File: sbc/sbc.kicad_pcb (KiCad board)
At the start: 4 copper layers, 111.8 x 76.2 mm, 38 parts, among them J1 USB_B_Micro, J2 EXP_1A, J3 EXP_1B, J4 EXP_2A, J5 EXP_2B, M1 M2, M2 M2, M3 M2, M4 M2, SW1 RESET, SW2 NMI, U1 DS1813, U2 WD65C02, U3 28C256, U4 62256, U5 7400, U6 WD65C22, U7 WD65C22, U8 74AHC1G08, U9 MAX6816, X1 2Mhz

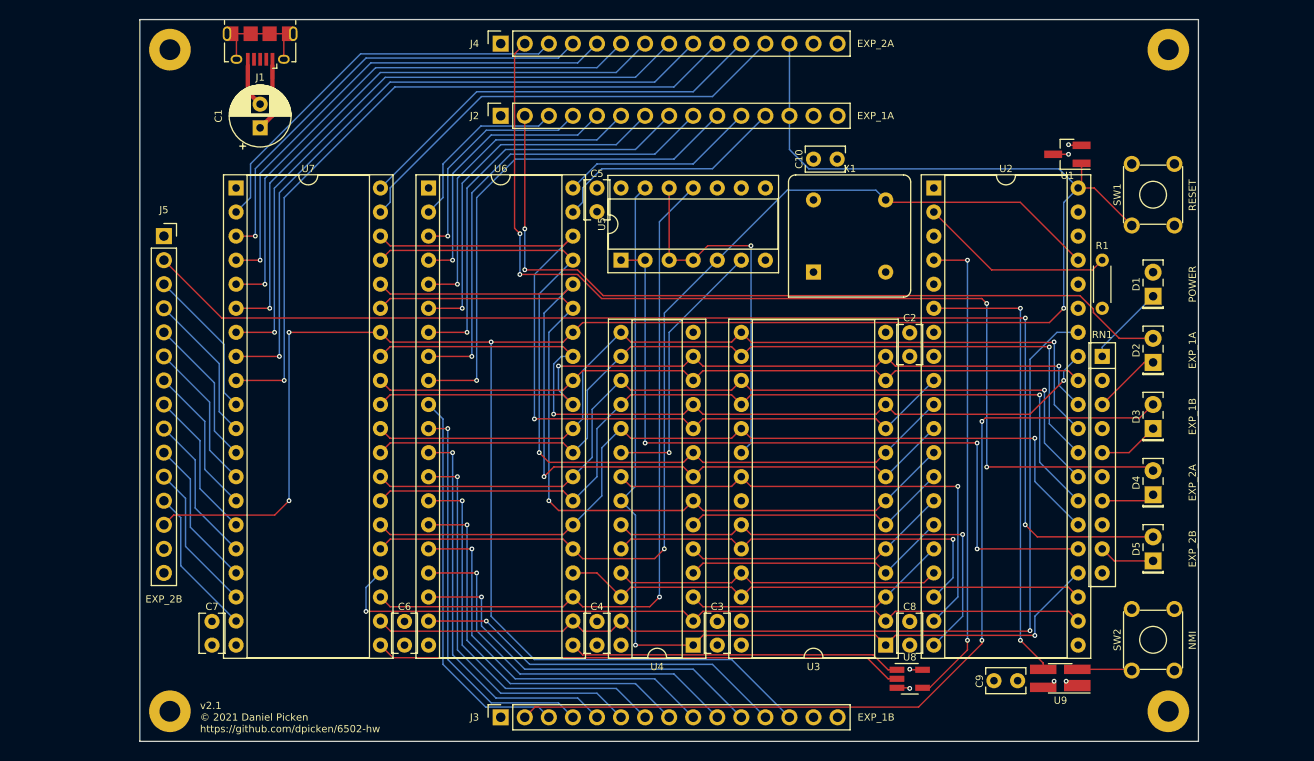
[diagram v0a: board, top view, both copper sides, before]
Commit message: SBC v2.2
Changes over v2:

  - Address space decode and IRQ glue logic moved into a PLD
  - Adds serial port and power via USB-C connector
  - Adds onboard microSD mass storage
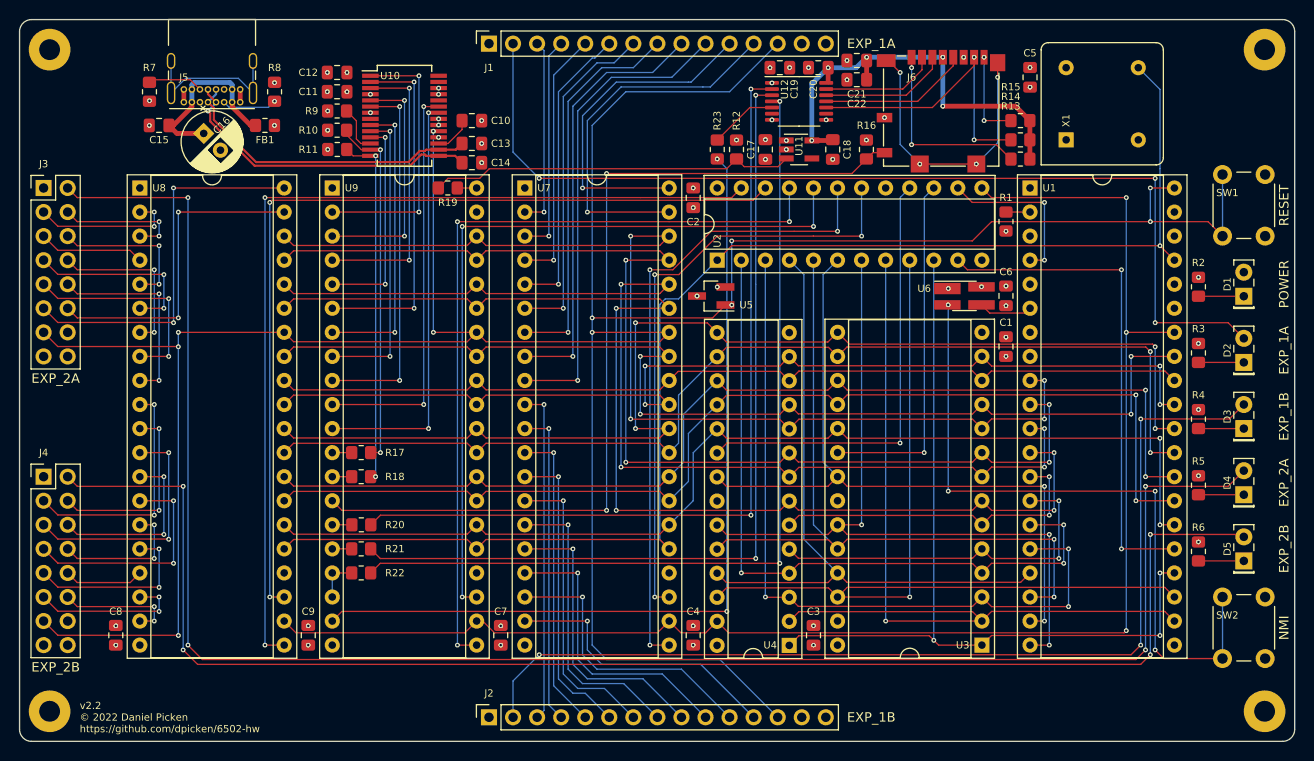
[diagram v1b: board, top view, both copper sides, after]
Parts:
- removed M1, M2, M3, M4: M2, mounting_hole:MountingHole_2.2mm_M2_Pad
- removed RN1: 100, resistor:R_Array_SIP10
- added C11: 0.1uF, Capacitor_SMD:C_0805_2012Metric_Pad1.18x1.45mm_HandSolder, F.Cu at (117.3, 58.4)
- added C12: 4.7uF, Capacitor_SMD:C_0805_2012Metric_Pad1.18x1.45mm_HandSolder, F.Cu at (117.3, 56.4)
- added C13: 47pF, Capacitor_SMD:C_0805_2012Metric_Pad1.18x1.45mm_HandSolder, F.Cu at (131.6, 63.9)
- added C14: 47pF, Capacitor_SMD:C_0805_2012Metric_Pad1.18x1.45mm_HandSolder, F.Cu at (131.6, 65.9)
- added C15: 10nF, Capacitor_SMD:C_0805_2012Metric_Pad1.18x1.45mm_HandSolder, F.Cu at (98.6, 62.0)
- added C16: 220uF, Capacitor_THT:CP_Radial_D6.3mm_P2.50mm, F.Cu at (103.3, 62.8)
- added C17: 1uF, Capacitor_SMD:C_0805_2012Metric_Pad1.18x1.45mm_HandSolder, F.Cu at (162.6, 64.5)
- added C18: 1uF, Capacitor_SMD:C_0805_2012Metric_Pad1.18x1.45mm_HandSolder, F.Cu at (169.7, 64.5)
- added C19: 0.1uF, Capacitor_SMD:C_0805_2012Metric_Pad1.18x1.45mm_HandSolder, F.Cu at (164.1, 55.9)
- added C20: 0.1uF, Capacitor_SMD:C_0805_2012Metric_Pad1.18x1.45mm_HandSolder, F.Cu at (168.1, 55.9)
- added C21: 0.1uF, Capacitor_SMD:C_0805_2012Metric_Pad1.18x1.45mm_HandSolder, F.Cu at (172.2, 55.1)
- added C22: 4.7uF, Capacitor_SMD:C_0805_2012Metric_Pad1.18x1.45mm_HandSolder, F.Cu at (172.2, 57.1)
- added FB1: FerriteBead, Resistor_SMD:R_0805_2012Metric_Pad1.20x1.40mm_HandSolder, F.Cu at (109.7, 62.0)
- added H1: MountingHole, MountingHole:MountingHole_2.2mm_M2_Pad, F.Cu at (87.0, 54.0)
- added H2: MountingHole, MountingHole:MountingHole_2.2mm_M2_Pad, F.Cu at (87.0, 123.8)
- added H3: MountingHole, MountingHole:MountingHole_2.2mm_M2_Pad, F.Cu at (215.3, 123.8)
- added H4: MountingHole, MountingHole:MountingHole_2.2mm_M2_Pad, F.Cu at (215.3, 54.0)
- added J6: 104031-0811, Project_Connector_Card:microSD_HC_Molex_104031-0811_HandSoler, F.Cu at (181.1, 60.5)
- added R10: 10K, Resistor_SMD:R_0805_2012Metric_Pad1.20x1.40mm_HandSolder, F.Cu at (117.3, 62.5)
- added R11: 10K, Resistor_SMD:R_0805_2012Metric_Pad1.20x1.40mm_HandSolder, F.Cu at (117.4, 64.5)
- added R12: 10K, Resistor_SMD:R_0805_2012Metric_Pad1.20x1.40mm_HandSolder, F.Cu at (159.5, 64.5)
- added R13: 10K, Resistor_SMD:R_0805_2012Metric_Pad1.20x1.40mm_HandSolder, F.Cu at (189.5, 65.5)
- added R14: 10K, Resistor_SMD:R_0805_2012Metric_Pad1.20x1.40mm_HandSolder, F.Cu at (189.5, 63.5)
- added R15: 10K, Resistor_SMD:R_0805_2012Metric_Pad1.20x1.40mm_HandSolder, F.Cu at (189.5, 61.5)
- added R16: 10K, Resistor_SMD:R_0805_2012Metric_Pad1.20x1.40mm_HandSolder, F.Cu at (173.2, 64.5)
- added R17: 30R, Resistor_SMD:R_0805_2012Metric_Pad1.20x1.40mm_HandSolder, F.Cu at (119.9, 96.5)
- added R18: 30R, Resistor_SMD:R_0805_2012Metric_Pad1.20x1.40mm_HandSolder, F.Cu at (119.9, 99.1)
- added R19: 30R, Resistor_SMD:R_0805_2012Metric_Pad1.20x1.40mm_HandSolder, F.Cu at (129.0, 68.6)
- added R2: 150R, Resistor_SMD:R_0805_2012Metric_Pad1.20x1.40mm_HandSolder, F.Cu at (208.3, 79.0)
- added R20: 30R, Resistor_SMD:R_0805_2012Metric_Pad1.20x1.40mm_HandSolder, F.Cu at (119.9, 104.1)
- added R21: 30R, Resistor_SMD:R_0805_2012Metric_Pad1.20x1.40mm_HandSolder, F.Cu at (119.9, 106.7)
- added R22: 30R, Resistor_SMD:R_0805_2012Metric_Pad1.20x1.40mm_HandSolder, F.Cu at (119.9, 109.2)
- added R23: 30R, Resistor_SMD:R_0805_2012Metric_Pad1.20x1.40mm_HandSolder, F.Cu at (157.5, 64.5)
- added R3: 150R, Resistor_SMD:R_0805_2012Metric_Pad1.20x1.40mm_HandSolder, F.Cu at (208.3, 86.0)
- added R4: 150R, Resistor_SMD:R_0805_2012Metric_Pad1.20x1.40mm_HandSolder, F.Cu at (208.3, 93.0)
- added R5: 150R, Resistor_SMD:R_0805_2012Metric_Pad1.20x1.40mm_HandSolder, F.Cu at (208.3, 100.0)
- added R6: 150R, Resistor_SMD:R_0805_2012Metric_Pad1.20x1.40mm_HandSolder, F.Cu at (208.3, 107.0)
- added R7: 5.1K, Resistor_SMD:R_0805_2012Metric_Pad1.20x1.40mm_HandSolder, F.Cu at (97.5, 58.4)
- added R8: 5.1K, Resistor_SMD:R_0805_2012Metric_Pad1.20x1.40mm_HandSolder, F.Cu at (110.7, 58.4)
- added R9: 10K, Resistor_SMD:R_0805_2012Metric_Pad1.20x1.40mm_HandSolder, F.Cu at (117.3, 60.5)
- added U10: FT245R, Package_SO:SSOP-28_5.3x10.2mm_P0.65mm, F.Cu at (124.5, 61.0)
- added U11: LD39015M33R, Package_TO_SOT_SMD:SOT-23-5_HandSoldering, F.Cu at (166.1, 64.5)
- added U12: TXU0304, Package_SO:TSSOP-14_4.4x5mm_P0.65mm, F.Cu at (166.1, 59.4)
- C1: value 220uf -> 0.1uF; footprint capacitor:CP_Radial_D6.3mm_P2.50mm -> Capacitor_SMD:C_0805_2012Metric_Pad1.18x1.45mm_HandSolder
- C10, C3, C4, C5, C6, C7, C8, C9: footprint capacitor:C_Rect_L4.0mm_W2.5mm_P2.50mm -> Capacitor_SMD:C_0805_2012Metric_Pad1.18x1.45mm_HandSolder
- C2: value 0.1uF -> 0.22uF; footprint capacitor:C_Rect_L4.0mm_W2.5mm_P2.50mm -> Capacitor_SMD:C_0805_2012Metric_Pad1.18x1.45mm_HandSolder
- D1, D2, D3, D4, D5: footprint led:LED_Rectangular_W5.0mm_H2.0mm -> LED_THT:LED_Rectangular_W5.0mm_H2.0mm
- J1: value USB_B_Micro -> EXP_1A; footprint connector_usb_handsoldering:USB_Micro-B_Amphenol_10118194_Horizontal_HandSoldering -> Connector_PinSocket_2.54mm:PinSocket_1x15_P2.54mm_Vertical
- J2: value EXP_1A -> EXP_1B; footprint connector:PinSocket_1x15_P2.54mm_Vertical -> Connector_PinSocket_2.54mm:PinSocket_1x15_P2.54mm_Vertical
- J3: value EXP_1B -> EXP_2A; footprint connector:PinSocket_1x15_P2.54mm_Vertical -> Connector_PinHeader_2.54mm:PinHeader_2x08_P2.54mm_Vertical
- J4: value EXP_2A -> EXP_2B; footprint connector:PinSocket_1x15_P2.54mm_Vertical -> Connector_PinHeader_2.54mm:PinHeader_2x08_P2.54mm_Vertical
- J5: value EXP_2B -> USB_C_USB2.0; footprint connector:PinSocket_1x15_P2.54mm_Vertical -> Connector_USB:USB_C_Receptacle_GCT_USB4085
- R1: value 1K -> 3K; footprint resistor:R_Axial_DIN0204_L3.6mm_D1.6mm_P5.08mm_Horizontal -> Resistor_SMD:R_0805_2012Metric_Pad1.20x1.40mm_HandSolder
- SW1, SW2: footprint switch:SW_TH_Tactile_Omron_B3F-10xx -> Button_Switch_THT:SW_PUSH_6mm_H4.3mm
- U1: value DS1813 -> WD65C02; footprint to_sot_smd:SOT-23_Handsoldering -> Package_DIP:DIP-40_W15.24mm_Socket
- U2: value WD65C02 -> ATF22V10C; footprint dip:DIP-40_W15.24mm_Socket -> Package_DIP:DIP-24_W7.62mm_Socket
- U3: footprint dip:DIP-28_W15.24mm_Socket -> Package_DIP:DIP-28_W15.24mm_Socket
- U4: value 62256 -> AS7C256B; footprint dip:DIP-28_W7.62mm_Socket -> Package_DIP:DIP-28_W7.62mm_Socket
- U5: value 7400 -> DS1813; footprint dip:DIP-14_W7.62mm_Socket -> Package_TO_SOT_SMD:SOT-23_Handsoldering
- U6: value WD65C22 -> MAX6816; footprint dip:DIP-40_W15.24mm_Socket -> Package_TO_SOT_SMD:SOT-143_Handsoldering
- U7: footprint dip:DIP-40_W15.24mm_Socket -> Package_DIP:DIP-40_W15.24mm_Socket
- U8: value 74AHC1G08 -> WD65C22; footprint to_sot_smd:SOT-23-5_HandSoldering -> Package_DIP:DIP-40_W15.24mm_Socket
- U9: value MAX6816 -> WD65C22; footprint to_sot_smd:SOT-143_Handsoldering -> Package_DIP:DIP-40_W15.24mm_Socket
- X1: value 2Mhz -> 8MHz; footprint oscillator:Oscillator_DIP-8 -> Oscillator:Oscillator_DIP-8
- moved U8 96.4 mm to (96.5, 68.6)
- moved U9 92.7 mm to (116.8, 68.6), turned to 0 degrees
- moved C8 83.8 mm to (94.0, 115.8)
- moved C1 82.1 mm to (188.0, 85.3)
- moved C9 75.0 mm to (114.3, 115.8), turned to 90 degrees
- moved J3 73.8 mm to (86.4, 68.6), turned to 0 degrees
- moved C6 73.4 mm to (188.0, 80.0), turned to -90 degrees
- moved J4 66.5 mm to (86.4, 99.1), turned to 0 degrees
- moved J2 63.5 mm to (133.4, 124.5)
- moved U6 57.7 mm to (183.6, 80.0)
- moved C5 47.2 mm to (190.5, 56.9)
- moved C10 36.3 mm to (131.6, 61.5)
- moved C7 30.5 mm to (134.6, 115.8)
- moved U7 30.5 mm to (137.2, 68.6)
- moved X1 30.1 mm to (194.3, 63.5)
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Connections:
- C10 pad 1: +5V -> Net-(C10-Pad1)
- J1 pad 2: Net-(J1-Pad2) -> EXP_1A_LED
- J1 pad 3: Net-(J1-Pad3) -> VIA1_PA0
- J1 pad 4: Net-(J1-Pad4) -> VIA1_PA1
- J1 pad 5: GND -> VIA1_PA2
- J1 pad 6: Net-(J1-Pad6) -> VIA1_PA3
- J2 pad 10: VIA1_PA7 -> VIA1_PB7
- J2 pad 11: VIA1_CA1 -> VIA1_CB1
- J2 pad 12: VIA1_CA2 -> VIA1_CB2
- J2 pad 13: RESET -> /RESET
- J2 pad 15: Net-(J2-Pad15) -> unconnected-(J2-Pad15)
- J2 pad 2: EXP_1A_LED -> EXP_1B_LED
- J2 pad 3: VIA1_PA0 -> VIA1_PB0
- J2 pad 4: VIA1_PA1 -> VIA1_PB1
- J2 pad 5: VIA1_PA2 -> VIA1_PB2
- J2 pad 6: VIA1_PA3 -> VIA1_PB3
- J2 pad 7: VIA1_PA4 -> VIA1_PB4
- J2 pad 8: VIA1_PA5 -> VIA1_PB5
- J2 pad 9: VIA1_PA6 -> VIA1_PB6
- J3 pad 10: VIA1_PB7 -> VIA2_PA7
- J3 pad 11: VIA1_CB1 -> VIA2_CA1
- J3 pad 12: VIA1_CB2 -> VIA2_CA2
- J3 pad 13: RESET -> /RESET
- J3 pad 15: Net-(J3-Pad15) -> unconnected-(J3-Pad15)
- J3 pad 2: EXP_1B_LED -> EXP_2A_LED
- J3 pad 3: VIA1_PB0 -> VIA2_PA0
- J3 pad 4: VIA1_PB1 -> VIA2_PA1
- J3 pad 5: VIA1_PB2 -> VIA2_PA2
- J3 pad 6: VIA1_PB3 -> VIA2_PA3
- J3 pad 7: VIA1_PB4 -> VIA2_PA4
- J3 pad 8: VIA1_PB5 -> VIA2_PA5
- J3 pad 9: VIA1_PB6 -> VIA2_PA6
- J4 pad 10: VIA2_PA7 -> VIA2_PB7
- J4 pad 11: VIA2_CA1 -> VIA2_CB1
- J4 pad 12: VIA2_CA2 -> VIA2_CB2
- J4 pad 13: RESET -> /RESET
- J4 pad 15: Net-(J4-Pad15) -> unconnected-(J4-Pad15)
- J4 pad 2: EXP_2A_LED -> EXP_2B_LED
- J4 pad 3: VIA2_PA0 -> VIA2_PB0
- J4 pad 4: VIA2_PA1 -> VIA2_PB1
- J4 pad 5: VIA2_PA2 -> VIA2_PB2
- J4 pad 6: VIA2_PA3 -> VIA2_PB3
- J4 pad 7: VIA2_PA4 -> VIA2_PB4
- J4 pad 8: VIA2_PA5 -> VIA2_PB5
- J4 pad 9: VIA2_PA6 -> VIA2_PB6
- R1 pad 1: Net-(R1-Pad1) -> +5V
- R1 pad 2: +5V -> Net-(R1-Pad2)
- SW1 pad 1: RESET -> /RESET
- SW1 pad 2: (no net) -> GND
- SW2 pad 2: (no net) -> GND
- U1 pad 1: RESET -> unconnected-(U1-Pad1)
- U1 pad 2: +5V -> Net-(R1-Pad2)
- U1 pad 3: GND -> unconnected-(U1-Pad3)
- U2 pad 1: Net-(U2-Pad1) -> PHI2
- U2 pad 10: /A1 -> A14
- U2 pad 11: /A2 -> A15
- U2 pad 12: /A3 -> GND
- U2 pad 13: /A4 -> /W
- U2 pad 14: /A5 -> /IRQ
- U2 pad 15: /A6 -> /ROM
- U2 pad 16: /A7 -> /RAM
- U2 pad 17: /A8 -> unconnected-(U2-Pad17)
- U2 pad 18: /A9 -> /VIA1
- U2 pad 19: /A10 -> /VIA1_IRQ
- U2 pad 2: Net-(R1-Pad1) -> A6
- U2 pad 20: /A11 -> /VIA3
- U2 pad 21: GND -> /VIA3_IRQ
- U2 pad 22: /A12 -> /VIA2
- U2 pad 23: /A13 -> /VIA2_IRQ
- U2 pad 24: /A14 -> +5V
- U2 pad 3: Net-(U2-Pad3) -> A7
- U2 pad 4: IRQ -> A8
- U2 pad 5: Net-(U2-Pad5) -> A9
- U2 pad 6: NMI -> A10
- U2 pad 7: Net-(U2-Pad7) -> A11
- U2 pad 8: +5V -> A12
- U2 pad 9: /A0 -> A13
- U3 pad 1: /A14 -> A14
- U3 pad 10: /A0 -> A0
- U3 pad 11: /D0 -> D0
- U3 pad 12: /D1 -> D1
- U3 pad 13: /D2 -> D2
- U3 pad 15: /D3 -> D3
- U3 pad 16: /D4 -> D4
- U3 pad 17: /D5 -> D5
- U3 pad 18: /D6 -> D6
- U3 pad 19: /D7 -> D7
- U3 pad 2: /A12 -> A12
- U3 pad 20: Net-(U3-Pad20) -> /ROM
- U3 pad 21: /A10 -> A10
- U3 pad 23: /A11 -> A11
- U3 pad 24: /A9 -> A9
- U3 pad 25: /A8 -> A8
- U3 pad 26: /A13 -> A13
- U3 pad 3: /A7 -> A7
- U3 pad 4: /A6 -> A6
- U3 pad 5: /A5 -> A5
- U3 pad 6: /A4 -> A4
- U3 pad 7: /A3 -> A3
- U3 pad 8: /A2 -> A2
- U3 pad 9: /A1 -> A1
- U4 pad 1: /A14 -> A14
- U4 pad 10: /A0 -> A0
- U4 pad 11: /D0 -> D0
- U4 pad 12: /D1 -> D1
- U4 pad 13: /D2 -> D2
- U4 pad 15: /D3 -> D3
- U4 pad 16: /D4 -> D4
- U4 pad 17: /D5 -> D5
- U4 pad 18: /D6 -> D6
- U4 pad 19: /D7 -> D7
- U4 pad 2: /A12 -> A12
- U4 pad 20: Net-(U4-Pad20) -> /RAM
- U4 pad 21: /A10 -> A10
- U4 pad 22: /A14 -> GND
- U4 pad 23: /A11 -> A11
- U4 pad 24: /A9 -> A9
- U4 pad 25: /A8 -> A8
- U4 pad 26: /A13 -> A13
- U4 pad 27: Net-(U2-Pad34) -> /W
- U4 pad 3: /A7 -> A7
- U4 pad 4: /A6 -> A6
- U4 pad 5: /A5 -> A5
- U4 pad 6: /A4 -> A4
- U4 pad 7: /A3 -> A3
- U4 pad 8: /A2 -> A2
- U4 pad 9: /A1 -> A1
- U5 pad 1: /A15 -> /RESET
- U5 pad 2: /A15 -> +5V
- U5 pad 3: Net-(U3-Pad20) -> GND
- U6 pad 2: VIA1_PA0 -> Net-(SW2-Pad1)
- U6 pad 3: VIA1_PA1 -> /NMI
- U6 pad 4: VIA1_PA2 -> +5V
- U7 pad 10: VIA2_PB0 -> VIA1_PB0
- U7 pad 11: VIA2_PB1 -> VIA1_PB1
- U7 pad 12: VIA2_PB2 -> VIA1_PB2
- U7 pad 13: VIA2_PB3 -> VIA1_PB3
- U7 pad 14: VIA2_PB4 -> VIA1_PB4
- U7 pad 15: VIA2_PB5 -> VIA1_PB5
- U7 pad 16: VIA2_PB6 -> VIA1_PB6
- U7 pad 17: VIA2_PB7 -> VIA1_PB7
- U7 pad 18: VIA2_CB1 -> VIA1_CB1
- U7 pad 19: VIA2_CB2 -> VIA1_CB2
- U7 pad 2: VIA2_PA0 -> VIA1_PA0
- U7 pad 21: VIA2_IRQ -> /VIA1_IRQ
- U7 pad 22: Net-(U2-Pad34) -> /W
- U7 pad 23: Net-(U5-Pad11) -> /VIA1
- U7 pad 24: /A12 -> +5V
- U7 pad 25: Net-(U2-Pad37) -> PHI2
- U7 pad 26: /D7 -> D7
- U7 pad 27: /D6 -> D6
- U7 pad 28: /D5 -> D5
- U7 pad 29: /D4 -> D4
- U7 pad 3: VIA2_PA1 -> VIA1_PA1
- U7 pad 30: /D3 -> D3
- U7 pad 31: /D2 -> D2
- U7 pad 32: /D1 -> D1
- U7 pad 33: /D0 -> D0
- U7 pad 34: RESET -> /RESET
- U7 pad 35: /A3 -> A3
- U7 pad 36: /A2 -> A2
- U7 pad 37: /A1 -> A1
- U7 pad 38: /A0 -> A0
- U7 pad 39: VIA2_CA2 -> VIA1_CA2
- U7 pad 4: VIA2_PA2 -> VIA1_PA2
- U7 pad 40: VIA2_CA1 -> VIA1_CA1
- U7 pad 5: VIA2_PA3 -> VIA1_PA3
- U7 pad 6: VIA2_PA4 -> VIA1_PA4
- U7 pad 7: VIA2_PA5 -> VIA1_PA5
- U7 pad 8: VIA2_PA6 -> VIA1_PA6
- U7 pad 9: VIA2_PA7 -> VIA1_PA7
- U8 pad 1: VIA1_IRQ -> GND
- U8 pad 2: VIA2_IRQ -> VIA2_PA0
- U8 pad 3: GND -> VIA2_PA1
- U8 pad 4: IRQ -> VIA2_PA2
- U8 pad 5: +5V -> VIA2_PA3
- U9 pad 2: Net-(SW2-Pad1) -> FT245R_D0
- U9 pad 3: NMI -> FT245R_D1
- U9 pad 4: +5V -> FT245R_D2
- X1 pad 1: Net-(X1-Pad1) -> unconnected-(X1-Pad1)
- X1 pad 5: Net-(U2-Pad37) -> PHI2
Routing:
- net /RESET: track 0.00 -> 337.7 mm, vias 0 -> 11
- net RESET: track 247.3 -> 0.00 mm, vias 4 -> 0
- net /W: track 0.00 -> 159.0 mm, vias 0 -> 3
- net PHI2: track 0.00 -> 145.8 mm, vias 0 -> 1
- net A3: track 0.00 -> 125.7 mm, vias 0 -> 4
- net D3: track 0.00 -> 124.4 mm, vias 0 -> 4
- net A1: track 0.00 -> 122.7 mm, vias 0 -> 4
- net A2: track 0.00 -> 118.6 mm, vias 0 -> 4
- net A0: track 0.00 -> 116.6 mm, vias 0 -> 4
- net D0: track 0.00 -> 115.5 mm, vias 0 -> 4
- net D6: track 0.00 -> 115.2 mm, vias 0 -> 2
- net D4: track 0.00 -> 114.9 mm, vias 0 -> 2
- net D5: track 0.00 -> 113.2 mm, vias 0 -> 2
- net D7: track 0.00 -> 113.2 mm, vias 0 -> 2
- net D2: track 0.00 -> 110.5 mm, vias 0 -> 4
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- added copper zone on In2.Cu, net +5V
- added copper zone on In1.Cu, net GND
- removed copper zone on In1.Cu, net +5V
- removed copper zone on In2.Cu, net GND
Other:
- board size 111.8 x 76.2 mm -> 134.6 x 76.2 mm
- net class Default removed
- net class Power removed
- rule pad_to_mask_clearance: 0.0508 -> 0
- board text added: "v2.2 © 2022 Daniel Picken https://github.com/dpicken/6502-hw"
- board text removed: "v2.1 © 2021 Daniel Picken https://github.com/dpicken/6502-hw"

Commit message: SBC v2.3
Fixes over v2.2:

  - SBC: Fix the VIA footprint: CA1 and CB1 are inputs
  - SBC: Move the microSD power enable line from (VIA3) CA1 (input) to CA2 (output)
  - Controller: connect LED enable
  - Controller: SMT switches
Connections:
- U9 pad 39: unconnected-(U9-Pad39) -> SD_PWR
- U9 pad 40: SD_PWR -> unconnected-(U9-Pad40)
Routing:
- net SD_PWR: track 2.04 -> 4.57 mm, vias 0 -> 2
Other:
- board text added: "v2.3 © 2022 Daniel Picken https://github.com/dpicken/6502-hw"
- board text removed: "v2.2 © 2022 Daniel Picken https://github.com/dpicken/6502-hw"
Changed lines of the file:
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@@
   (title_block
     (title "6502 SBC")
-    (date "2022-03-08")
-    (rev "2.2")
+    (date "2022-04-02")
+    (rev "2.3")
   )
   (layers
@@
   (net 126 "VIA_SPI_SCLK")
   (net 127 "Net-(J6-Pad1)")
-  (net 128 "unconnected-(U9-Pad39)")
+  (net 128 "unconnected-(U9-Pad40)")
   (net 129 "Net-(J6-Pad8)")
   (net 130 "Net-(R12-Pad1)")
@@
       (net 34 "VIA1_PB7") (pinfunction "PB7") (pintype "bidirectional"))
     (pad "18" thru_hole oval locked (at 0 43.18) (size 1.6 1.6) (drill 0.8) (layers *.Cu *.Mask)
-      (net 35 "VIA1_CB1") (pinfunction "CB1") (pintype "bidirectional"))
+      (net 35 "VIA1_CB1") (pinfunction "CB1") (pintype "input"))
     (pad "19" thru_hole oval locked (at 0 45.72) (size 1.6 1.6) (drill 0.8) (layers *.Cu *.Mask)
       (net 36 "VIA1_CB2") (pinfunction "CB2") (pintype "bidirectional"))
@@
       (net 24 "VIA1_CA2") (pinfunction "CA2") (pintype "bidirectional"))
     (pad "40" thru_hole oval locked (at 15.24 0) (size 1.6 1.6) (drill 0.8) (layers *.Cu *.Mask)
-      (net 23 "VIA1_CA1") (pinfunction "CA1") (pintype "bidirectional"))
+      (net 23 "VIA1_CA1") (pinfunction "CA1") (pintype "input"))
     (model "${KICAD6_3DMODEL_DIR}/Package_DIP.3dshapes/DIP-40_W15.24mm_Socket.wrl"
       (offset (xyz 0 0 0))
@@
       (net 126 "VIA_SPI_SCLK") (pinfunction "PB7") (pintype "bidirectional"))
     (pad "18" thru_hole oval locked (at 0 43.18) (size 1.6 1.6) (drill 0.8) (layers *.Cu *.Mask)
-      (net 126 "VIA_SPI_SCLK") (pinfunction "CB1") (pintype "bidirectional"))
+      (net 126 "VIA_SPI_SCLK") (pinfunction "CB1") (pintype "input"))
     (pad "19" thru_hole oval locked (at 0 45.72) (size 1.6 1.6) (drill 0.8) (layers *.Cu *.Mask)
       (net 124 "VIA_SPI_MISO") (pinfunction "CB2") (pintype "bidirectional"))
@@
       (net 81 "A0") (pinfunction "RS0") (pintype "input"))
     (pad "39" thru_hole oval locked (at 15.24 2.54) (size 1.6 1.6) (drill 0.8) (layers *.Cu *.Mask)
-      (net 128 "unconnected-(U9-Pad39)") (pinfunction "CA2") (pintype "bidirectional+no_connect"))
+      (net 146 "SD_PWR") (pinfunction "CA2") (pintype "bidirectional"))
     (pad "40" thru_hole oval locked (at 15.24 0) (size 1.6 1.6) (drill 0.8) (layers *.Cu *.Mask)
-      (net 146 "SD_PWR") (pinfunction "CA1") (pintype "bidirectional"))
+      (net 128 "unconnected-(U9-Pad40)") (pinfunction "CA1") (pintype "input+no_connect"))
     (model "${KICAD6_3DMODEL_DIR}/Package_DIP.3dshapes/DIP-40_W15.24mm_Socket.wrl"
       (offset (xyz 0 0 0))
@@
       (net 56 "VIA2_PB7") (pinfunction "PB7") (pintype "bidirectional"))
     (pad "18" thru_hole oval locked (at 0 43.18) (size 1.6 1.6) (drill 0.8) (layers *.Cu *.Mask)
-      (net 57 "VIA2_CB1") (pinfunction "CB1") (pintype "bidirectional"))
+      (net 57 "VIA2_CB1") (pinfunction "CB1") (pintype "input"))
     (pad "19" thru_hole oval locked (at 0 45.72) (size 1.6 1.6) (drill 0.8) (layers *.Cu *.Mask)
       (net 58 "VIA2_CB2") (pinfunction "CB2") (pintype "bidirectional"))
@@
       (net 47 "VIA2_CA2") (pinfunction "CA2") (pintype "bidirectional"))
     (pad "40" thru_hole oval locked (at 15.24 0) (size 1.6 1.6) (drill 0.8) (layers *.Cu *.Mask)
-      (net 46 "VIA2_CA1") (pinfunction "CA1") (pintype "bidirectional"))
+      (net 46 "VIA2_CA1") (pinfunction "CA1") (pintype "input"))
     (model "${KICAD6_3DMODEL_DIR}/Package_DIP.3dshapes/DIP-40_W15.24mm_Socket.wrl"
       (offset (xyz 0 0 0))
@@
   (gr_arc (start 217.17 50.8) (mid 218.068026 51.171974) (end 218.44 52.07) (layer "Edge.Cuts") (width 0.127))
   (gr_rect (start 101.6 -61.8825) (end 122.174 -46.0675) (layer "F.Fab") (width 0.127) (fill none))
-  (gr_text "v2.2\n© 2022 Daniel Picken\nhttps://github.com/dpicken/6502-hw" (at 90.17 124.46) (layer "F.SilkS")
+  (gr_text "v2.3\n© 2022 Daniel Picken\nhttps://github.com/dpicken/6502-hw" (at 90.17 124.46) (layer "F.SilkS")
     (effects (font (size 0.762 0.762) (thickness 0.127)) (justify left))
   )
@@
   (via (at 185.645 61.468) (size 0.508) (drill 0.254) (layers "F.Cu" "B.Cu") (net 129))
   (segment (start 185.645 54.777) (end 185.645 61.468) (width 0.127) (layer "B.Cu") (net 129))
+  (segment (start 135.128 67.056) (end 129.556 67.056) (width 0.127) (layer "F.Cu") (net 130))
   (segment (start 160.32702 66.33102) (end 163.90098 66.33102) (width 0.127) (layer "F.Cu") (net 130))
-  (segment (start 158.48 66.548) (end 133.409282 66.548) (width 0.127) (layer "F.Cu") (net 130))
-  (segment (start 132.393282 67.564) (end 129.048 67.564) (width 0.127) (layer "F.Cu") (net 130))
+  (segment (start 129.556 67.056) (end 128.032 68.58) (width 0.127) (layer "F.Cu") (net 130))
   (segment (start 163.90098 66.33102) (end 164.766 65.466) (width 0.127) (layer "F.Cu") (net 130))
-  (segment (start 133.409282 66.548) (end 132.393282 67.564) (width 0.127) (layer "F.Cu") (net 130))
   (segment (start 159.512 65.516) (end 160.32702 66.33102) (width 0.127) (layer "F.Cu") (net 130))
-  (segment (start 129.048 67.564) (end 128.032 68.58) (width 0.127) (layer "F.Cu") (net 130))
+  (segment (start 158.48 66.548) (end 135.636 66.548) (width 0.127) (layer "F.Cu") (net 130))
+  (segment (start 135.636 66.548) (end 135.128 67.056) (width 0.127) (layer "F.Cu") (net 130))
   (segment (start 159.512 65.516) (end 158.48 66.548) (width 0.127) (layer "F.Cu") (net 130))
   (segment (start 161.036 103.124) (end 121.92 103.124) (width 0.127) (layer "F.Cu") (net 131))
@@
   (via (at 145.796 67.056) (size 0.508) (drill 0.254) (layers "F.Cu" "B.Cu") (net 145))
   (segment (start 145.796 102.616) (end 145.796 67.056) (width 0.127) (layer "B.Cu") (net 145))
-  (segment (start 130.032 68.58) (end 132.075 68.58) (width 0.127) (layer "F.Cu") (net 146))
+  (segment (start 132.075 71.12) (end 130.048 71.12) (width 0.127) (layer "F.Cu") (net 146))
+  (via (at 130.032 68.58) (size 0.508) (drill 0.254) (layers "F.Cu" "B.Cu") (net 146))
+  (via (at 130.048 71.12) (size 0.508) (drill 0.254) (layers "F.Cu" "B.Cu") (net 146))
+  (segment (start 130.048 71.12) (end 130.048 68.596) (width 0.127) (layer "B.Cu") (net 146))
+  (segment (start 130.048 68.596) (end 130.032 68.58) (width 0.127) (layer "B.Cu") (net 146))
   (segment (start 129.062 63.885) (end 130.5345 62.4125) (width 0.127) (layer "F.Cu") (net 148))
   (segment (start 128.06 63.885) (end 129.062 63.885) (width 0.127) (layer "F.Cu") (net 148))
